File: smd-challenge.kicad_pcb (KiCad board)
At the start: 2 copper layers, 41.3 x 31.8 mm, 25 parts, among them J1 DX07S016JA1R1500, J2 Conn_01x05, U1 MIC5504-3.3YM5, U2 ATSAMD21E15B-M, Y1 FA-238 16.0000MB-K3

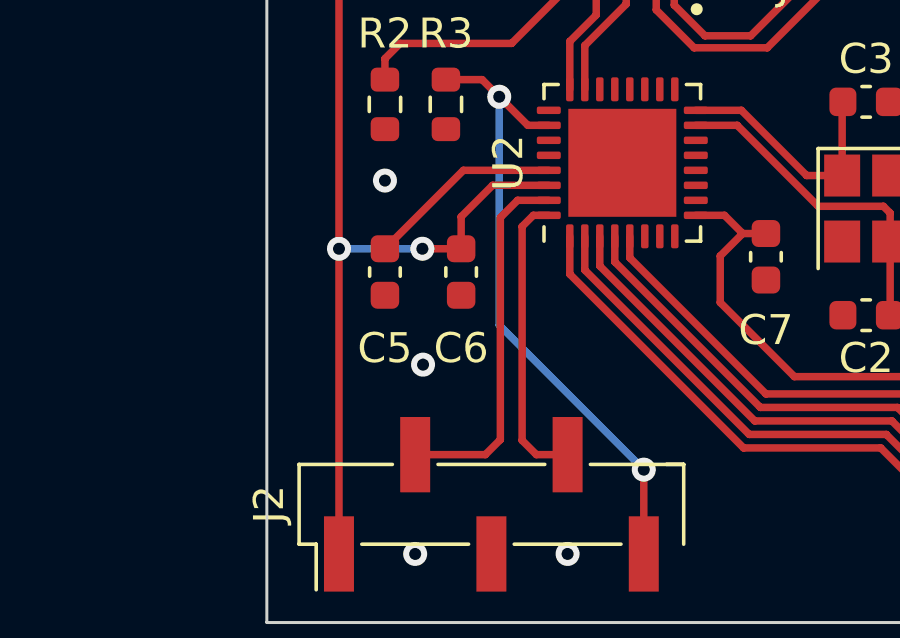
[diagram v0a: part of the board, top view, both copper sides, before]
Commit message: Add pull-up resistor on SWCLK per Microchip docs
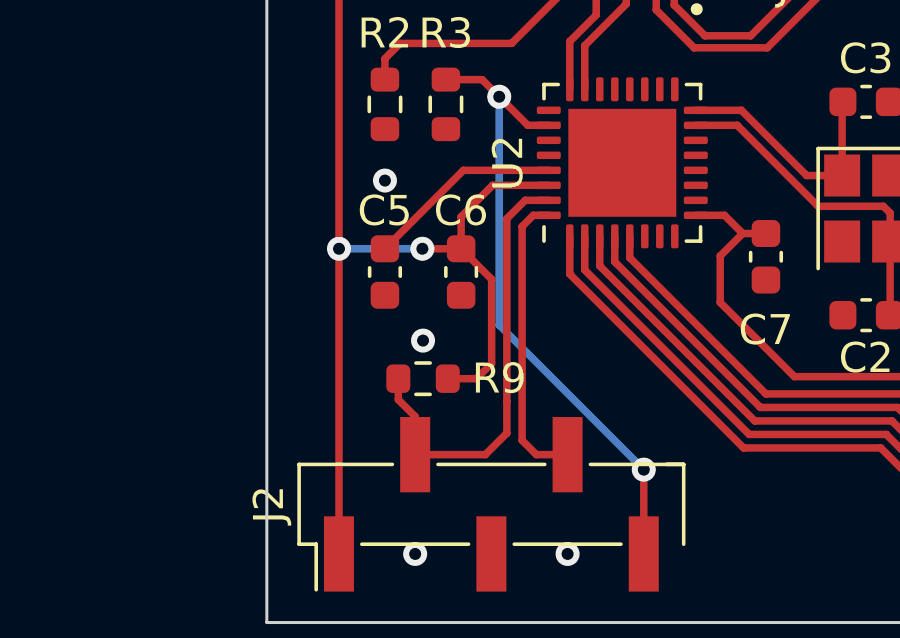
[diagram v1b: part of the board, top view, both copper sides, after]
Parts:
- added R9: 1k, Resistor_SMD:R_0603_1608Metric, F.Cu at (125.2, 61.5)
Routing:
- net +3V3: track 116.8 -> 122.7 mm
- net /SWCLK: track 12.3 -> 14.9 mm

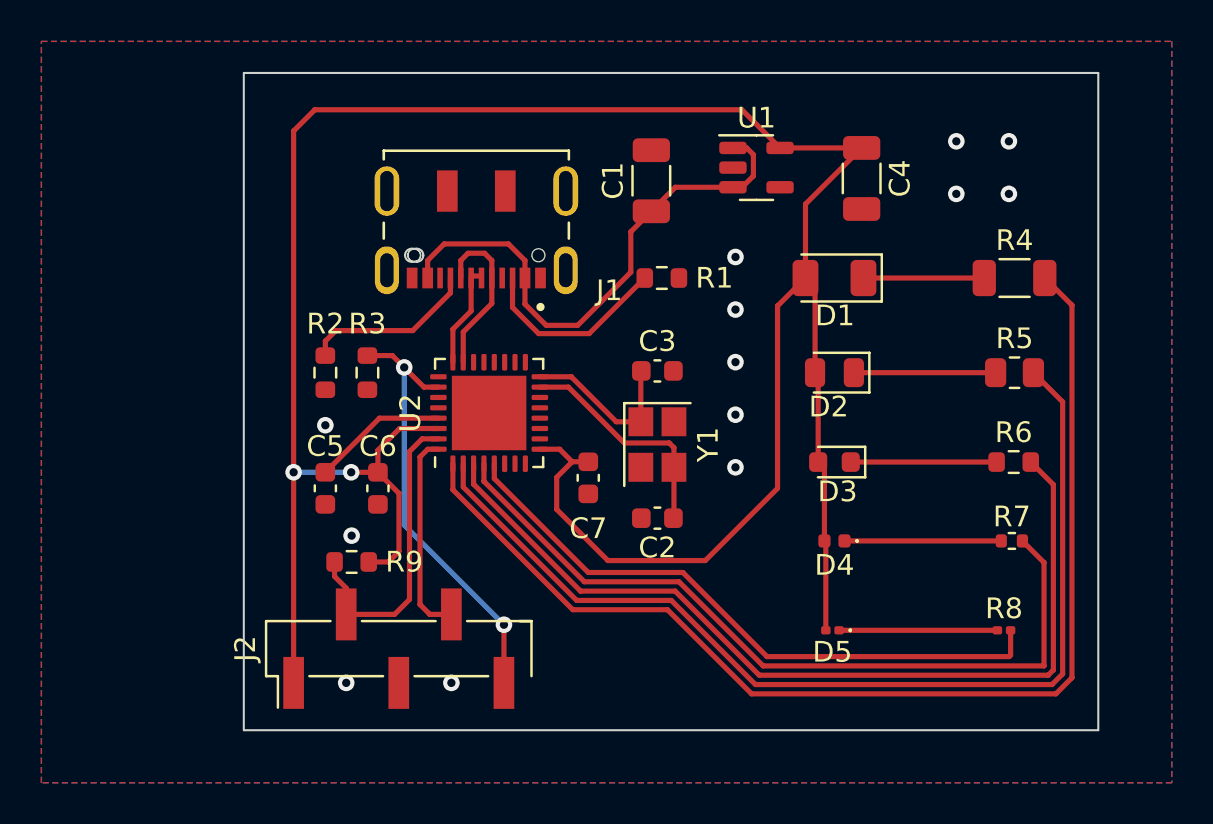
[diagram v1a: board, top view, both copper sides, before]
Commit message: Nudge the USB connector closer to the edge of the board so it's possible to plug in, and adjust some traces for symmetry
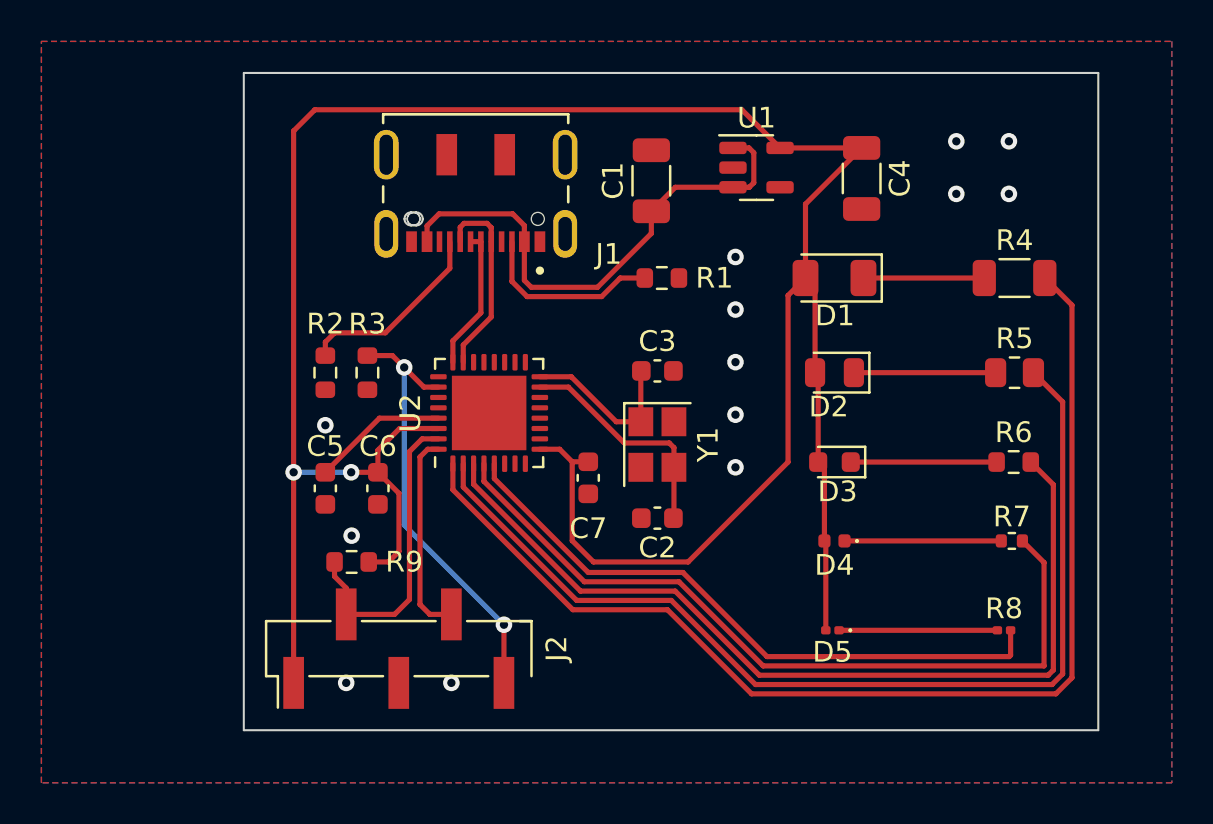
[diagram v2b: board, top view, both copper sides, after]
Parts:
- moved J1 1.76 mm to (131.2, 44.9)
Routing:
- net Net-(J1-Pad6): track 4.93 -> 6.89 mm
- net Net-(J1-Pad5): track 8.03 -> 9.42 mm
- net Net-(J1-Pad9): track 8.43 -> 9.43 mm
- net +5V: track 25.4 -> 24.6 mm
- net +3V3: track 122.7 -> 122.1 mm

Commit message: Add text to the back layer.
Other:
- board text added: "ATSAMD21E15B-M LED demo board"
- board text added: "© 2021 Matt Mullins"
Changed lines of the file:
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@@
   )
   (gr_rect (start 120.015 37.846) (end 161.29 69.596) (layer "Edge.Cuts") (width 0.1) (fill none))
+  (gr_text "© 2021 Matt Mullins" (at 140.6525 67.818) (layer "B.SilkS")
+    (effects (font (size 1.5 1.5) (thickness 0.3)) (justify mirror))
+  )
+  (gr_text "ATSAMD21E15B-M LED\ndemo board" (at 140.6525 53.721) (layer "B.SilkS")
+    (effects (font (size 1.5 1.5) (thickness 0.3)) (justify mirror))
+  )
   (via (at 143.764 49.276) (size 0.8) (drill 0.4) (layers "F.Cu" "B.Cu") (free) (net 1))
   (via (at 123.952 54.864) (size 0.8) (drill 0.4) (layers "F.Cu" "B.Cu") (free) (net 1))

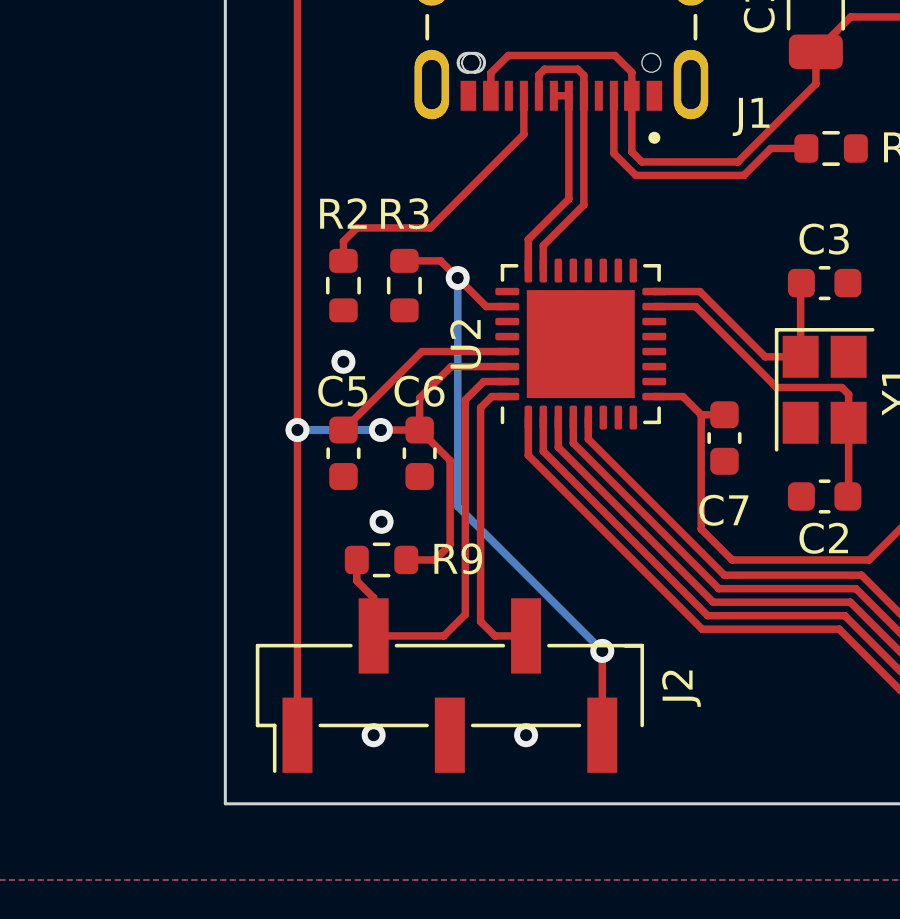
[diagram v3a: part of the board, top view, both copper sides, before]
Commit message: /NRST should be connected to a pull-UP
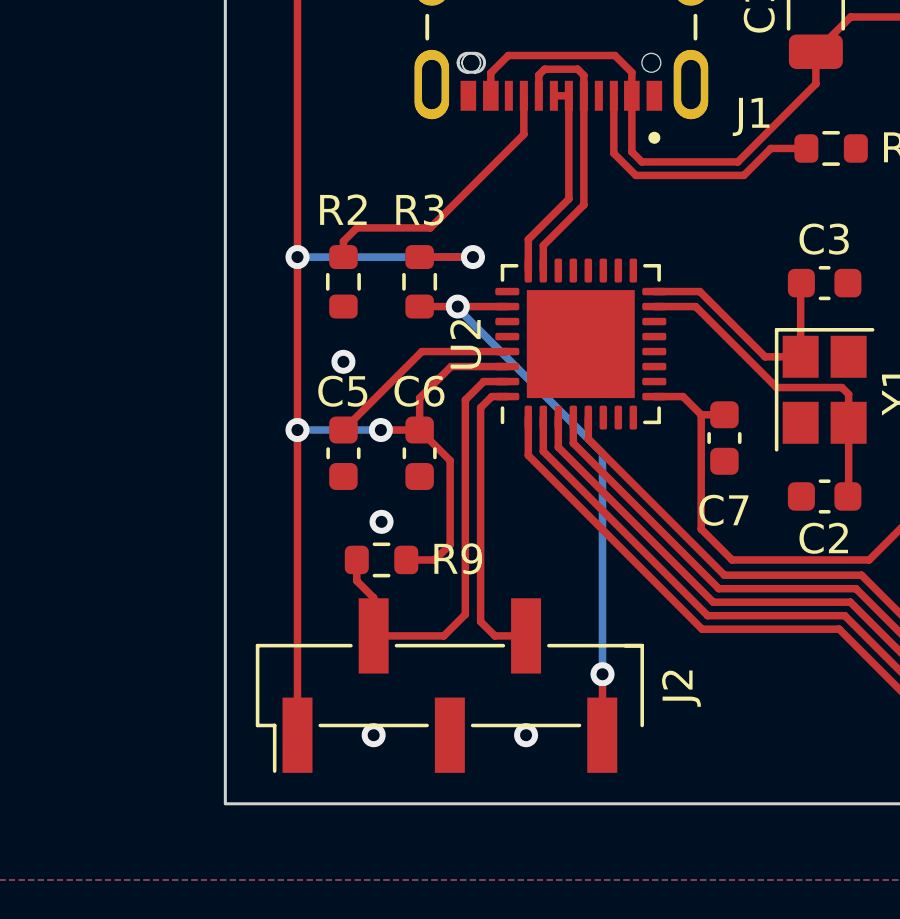
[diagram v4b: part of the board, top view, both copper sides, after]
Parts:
- C2, C3: value 12p -> 28p
- D1: value LED -> RED
- D2: value LED -> ORANGE
- D3: value LED -> YELLOW
- D4: value LED -> GREEN
- D5: value LED -> BLUE
- Y1: value FA-238 16.0000MB-K3 -> ECS-160-18-33QZ-ADS-TR
- moved R3 0.52 mm to (126.5, 52.2)
- moved R2 0.13 mm to (124.0, 52.2)
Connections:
- R3 pad 1: /NRST -> +3V3
- R3 pad 2: GND -> /NRST
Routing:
- net +3V3: track 122.1 -> 129.8 mm, vias 2 -> 4
- net /NRST: track 21.3 -> 19.2 mm
